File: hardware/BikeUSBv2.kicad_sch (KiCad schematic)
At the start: 51 parts, among them J1 TYPE-C-31-M-16, J2 JST S2B-EH(LF)(SN), SW1 1TS002E-2500-2501-CT, SW2 1TS002E-2500-2501-CT, U1 TPS63020DSJR, U2 ATtiny1616-M, U3 FUSB302B10MPX, U4 HT7550-2, U5 TPS259251

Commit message: add info note to sch
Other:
- note added: "This Board can be configured: * device power info - Analog-only with R1&R2 - Smart with U3 * IC supply - regulated and protected by U4 - unprotected (DNP U4, bridge JP2) not recommended, U5 might allow higher than 6V which is absolute maximum for U2&U3"
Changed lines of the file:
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@@
     (stroke (width 0) (type default))
   )
-  (rectangle (start 16.51 16.51) (end 62.865 57.15)
+  (rectangle (start 16.51 17) (end 62.865 57.15)
     (stroke (width 0) (type default))
     (fill (type none))
   )
-  (rectangle (start 127 19.05) (end 203.835 100.33)
+  (rectangle (start 127 17) (end 203.835 100.33)
     (stroke (width 0) (type default))
     (fill (type none))
@@
     (fill (type none))
   )
+  (rectangle (start 65 17) (end 126 57)
+    (stroke (width 0) (type default))
+    (fill (type none))
+  )
   (rectangle (start 16.51 61.595) (end 105.41 99.695)
     (stroke (width 0) (type default))
     (fill (type none))
   )
-  (text "the smarts" (at 98.425 111.125 0)
+  (text "the smarts" (at 100 110 0)
     (effects (font (size 1.27 1.27)) (justify left bottom))
   )
@@
     (effects (font (size 1.27 1.27)) (justify left bottom))
   )
-  (text "USB Type C" (at 121.285 151.13 0)
+  (text "USB Type C" (at 116 110 0)
     (effects (font (size 1.27 1.27)) (justify left bottom))
   )
-  (text "5V Regulator" (at 188.595 23.495 0)
+  (text "5V Regulator" (at 190 21 0)
     (effects (font (size 1.27 1.27)) (justify left bottom))
   )
@@
     (effects (font (size 1.27 1.27)) (justify left bottom))
   )
+  (text "This Board can be configured:\n* device power info\n  - Analog-only with R1&R2\n  - Smart with U3\n* IC supply\n  - regulated and protected by U4\n  - unprotected\n    (DNP U4, bridge JP2)\n    not recommended, U5 might allow\n    higher than 6V which is\n    absolute maximum for U2&U3"
+    (at 66 55 0)
+    (effects (font (size 2 2)) (justify left bottom))
+  )
   (text "analog" (at 163.83 118.745 0)

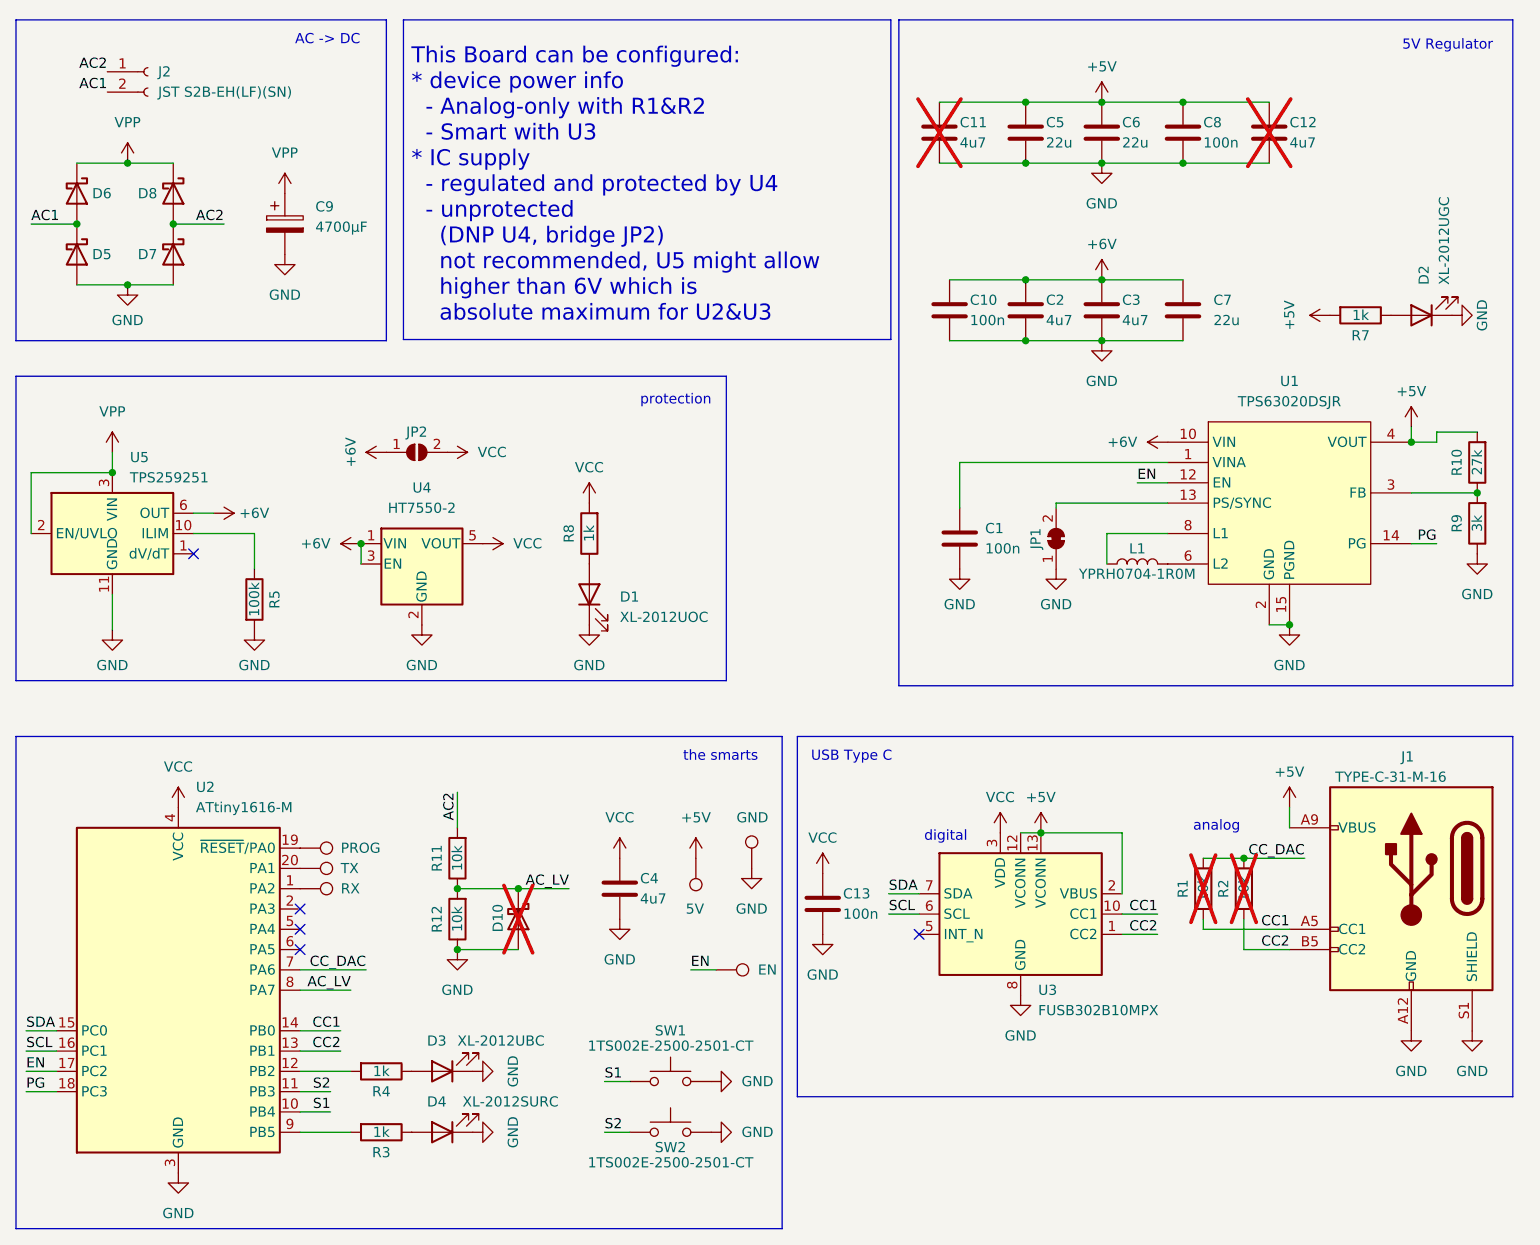
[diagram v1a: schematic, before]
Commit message: added resistor required in DS
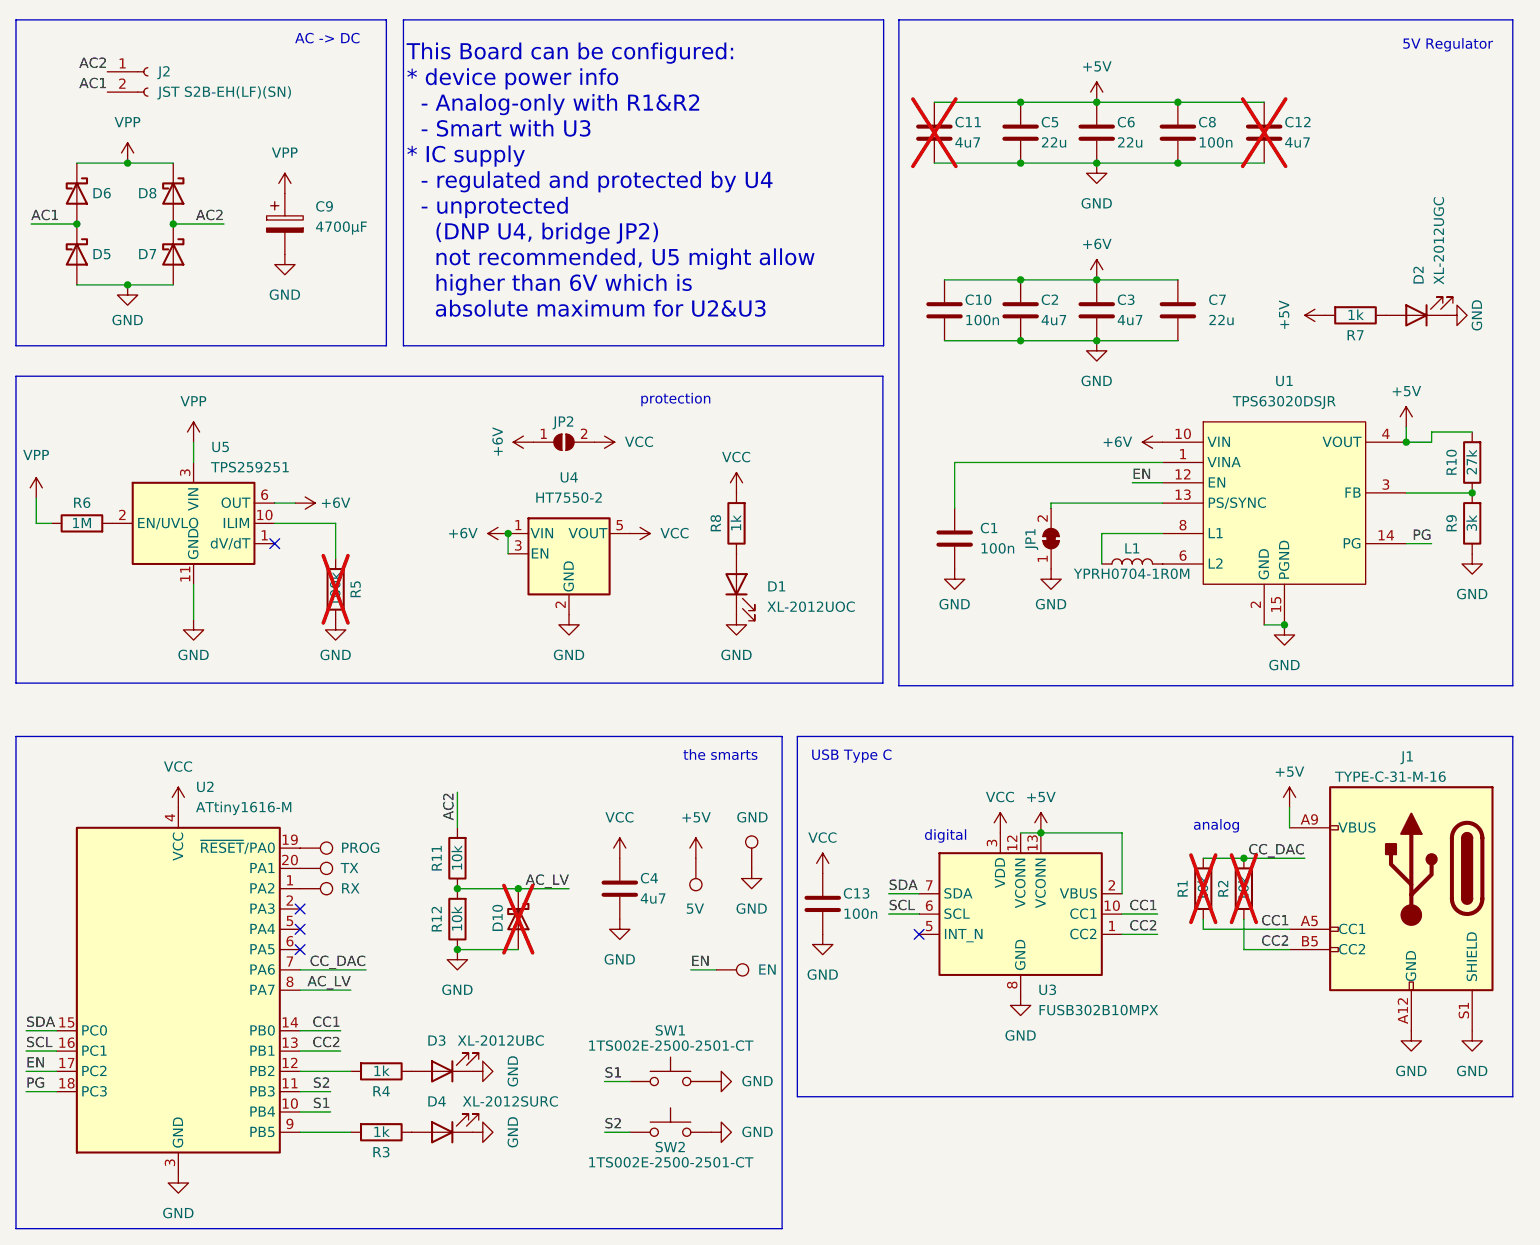
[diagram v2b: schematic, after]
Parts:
- added R6: 1M, Resistor_SMD:R_0805_2012Metric_Pad1.20x1.40mm_HandSolder, symbol Device:R
- R5: now not fitted
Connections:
- net VPP: now also R6.1; no longer U5.2 (EN/UVLO)
- new net: R6.2, U5.2 (EN/UVLO)
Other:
- moved on the sheet: C1, C10, C11, C12, C2, C3, C5, C6, C7, C8, D1, D2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

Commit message: make schematic look nicer
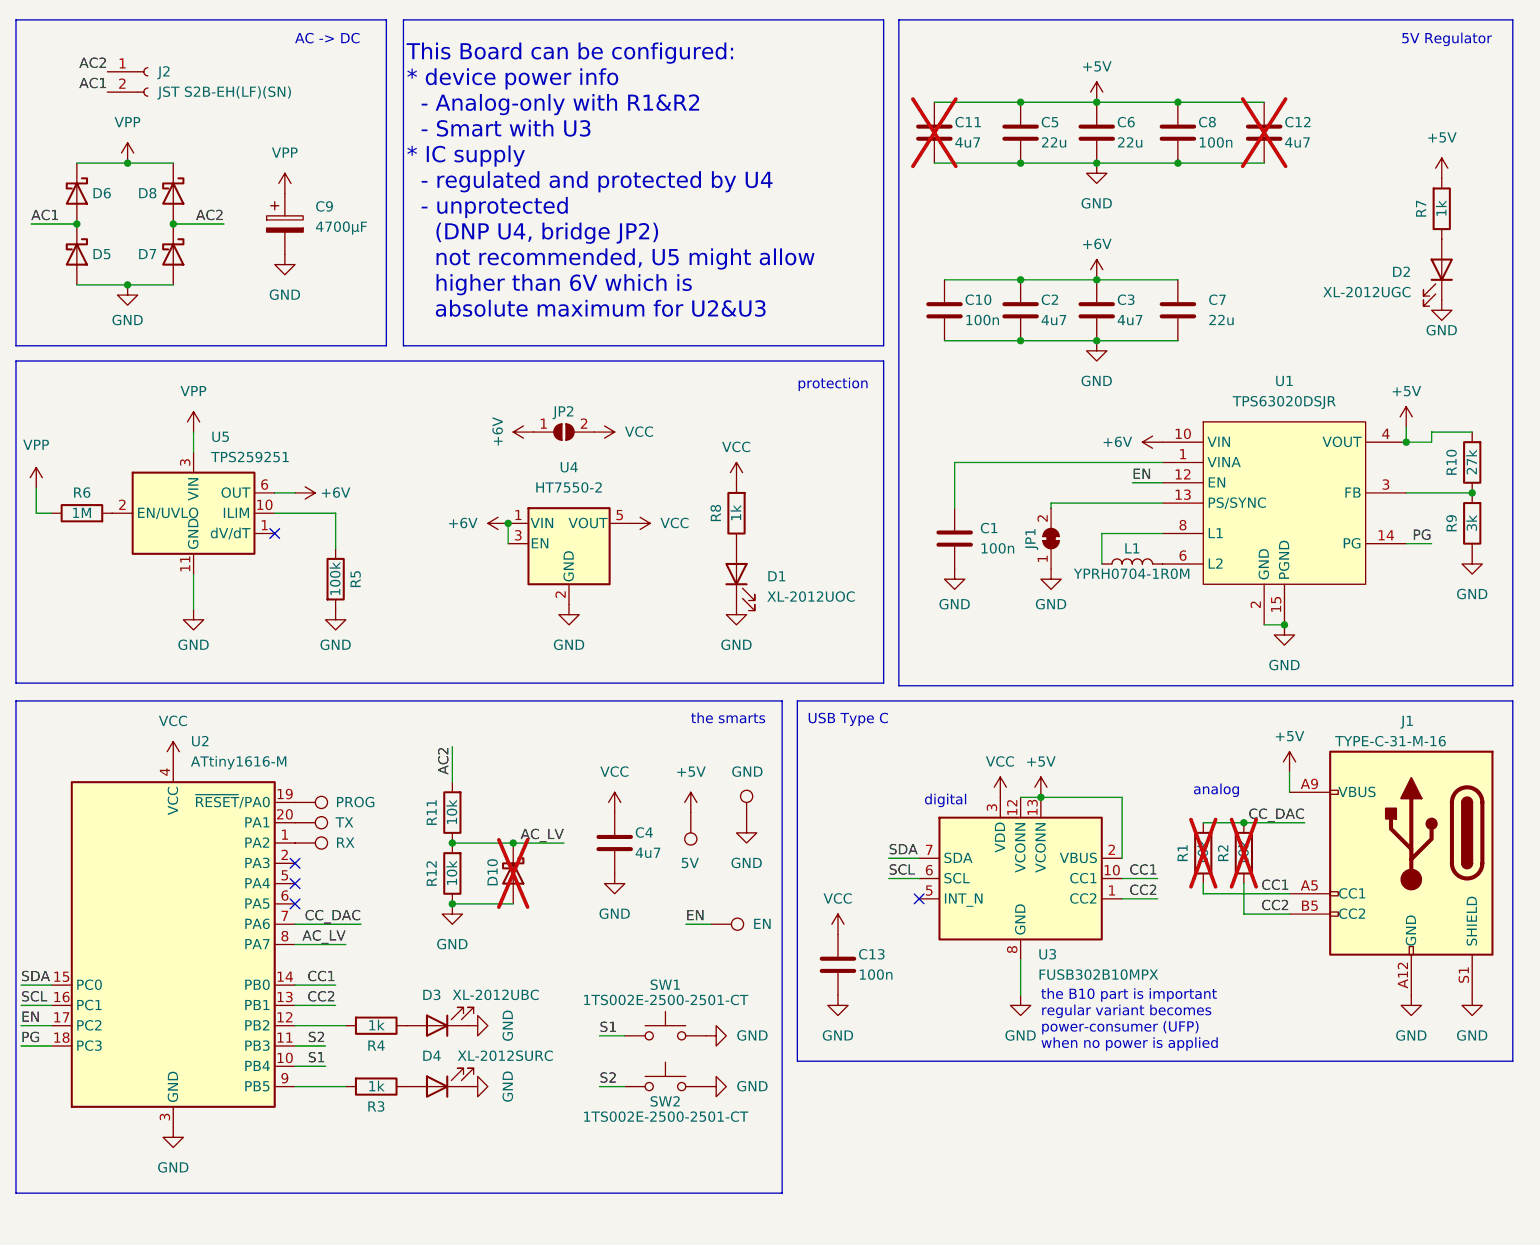
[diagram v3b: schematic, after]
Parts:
- R5: now fitted
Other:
- note added: "the B10 part is important regular variant becomes power-consumer (UFP) when no power is applied"
- moved on the sheet: C13, C4, D1, D10, D2, D3, D4, J1, JP2, R1, R11, R12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

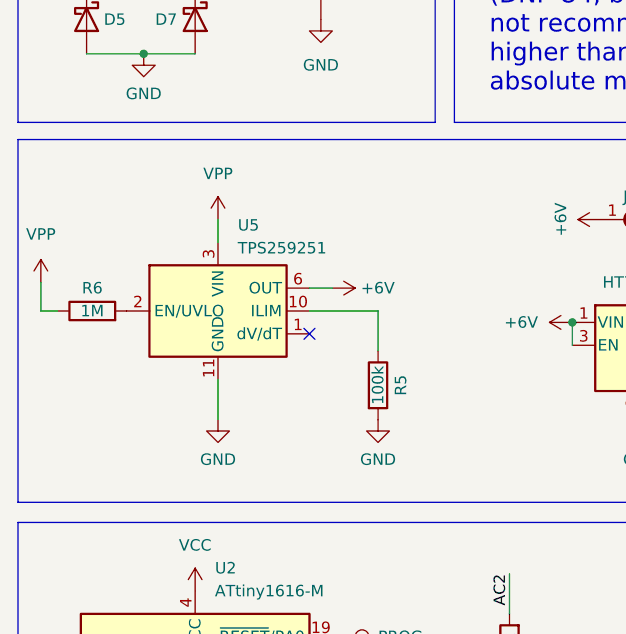
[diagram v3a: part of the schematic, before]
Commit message: switch eFuse IC in design
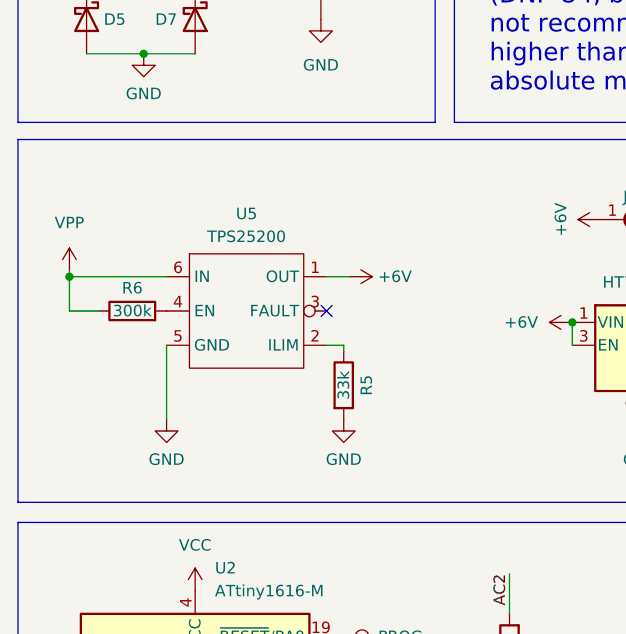
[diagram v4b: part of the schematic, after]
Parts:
- removed U5: TPS259251, Package_SON:VSON-10-1EP_3x3mm_P0.5mm_EP1.65x2.4mm_ThermalVias, symbol Power_Management:TPS2592xx
- added U5: TPS25200, Package_SON:WSON-6-1EP_2x2mm_P0.65mm_EP1x1.6mm_ThermalVias, symbol H3_IC:TPS25200
- R5: value 100k -> 33k; LCSC (none) -> C706276
- R6: value 1M -> 300k; LCSC (none) -> C865386
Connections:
- net +6V: now also U5.1 (OUT)
- net GND: now also U5.5 (GND), U5.7 (GND)
- net VPP: now also U5.6 (IN)
- net at R6.2: now also U5.4 (EN)
- net at R5.1: now also U5.2 (ILIM)
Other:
- moved on the sheet: R5, R6
